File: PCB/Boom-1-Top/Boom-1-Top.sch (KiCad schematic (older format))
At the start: 983 parts, among them J1 DEBUG, J10 PIC_DEBUG, J11 PIC_DEBUG, J12 PIC_DEBUG, J13 PIC_DEBUG, J14 PIC_DEBUG, J15 USB_B_Micro, J16 SD_Card, J17 BT_DEBUG, J18 12V Supply, J19 3V3 Bypass, J2 MIDI IN, J20 5V Bypass, J21 Env +12V Supply, J22 Env -12V Supply, J23 OLEDConn, J3 MIDI OUT, J37 Osc1Conn, J38 Osc2Conn, J39 SubNoiseConn, J4 PIC_DEBUG, J40 FiltConn2, J41 EnvGenConn2, J42 EnvGenConn1, J43 FXConn1, J44 FiltConn1, J45 FXConn2, J46 EnvGenConn3, J5 PIC_DEBUG, J6 PIC_DEBUG, J7 PIC_DEBUG, J8 PIC_DEBUG, J9 PIC_DEBUG, Q1 AO3401A, Q2 AO3401A, SW1 Osc1SawEncoder, SW10 SubToOsc2FiltEncoder, SW11 Osc1ToOsc2FiltEncoder, SW12 Osc1FiltFreqEncoder, SW13 Osc2FiltFreqEncoder, SW14 SubFiltFreqEncoder, SW15 OscFiltEnvAttackEncoder, SW16 SubFiltEnvAttackEncoder, SW17 Osc1FiltResEncoder, SW18 Osc2FiltResEncoder, SW19 SubFiltResEncoder, SW2 Osc1SqrEncoder, SW20 OscFiltEnvDecayEncoder, SW21 SubFiltEnvDecayEncoder, SW22 OscFiltEnvSustainEncoder, SW23 SubFiltEnvSustainEncoder, SW24 Osc1DriveEncoder, SW25 Osc2DistortionEncoder, SW26 OscFiltEnvReleaseEncoder, SW27 SubFiltEnvReleaseEncoder, SW28 FXWetDryEncoder, SW29 SubAmpEnvAttackEncoder, SW3 Rotary_Encoder, SW30 OscAmpEnvAttackEncoder, SW31 FXControl1Encoder, SW32 SubAmpEnvDecayEncoder, SW33 OscAmpEnvDecayEncoder, SW34 FXControl2Encoder, SW35 SubAmpEnvSustainEncoder, SW36 OscAmpEnvSustainEncoder, SW37 FXControl3Encoder, SW38 FXFeedbackEncoder, SW39 SubAmpEnvReleaseEncoder, SW4 Rotary_Encoder_Switch, SW40 OscAmpEnvReleaseEncoder, SW41 Reset, SW42 SW_Push, SW43 Reset, SW44 SW_Push, SW45 SW_Push, SW46 SW_Push, SW47 SW_Push, SW48 SW_Push, SW49 SW_Push, SW5 Rotary_Encoder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

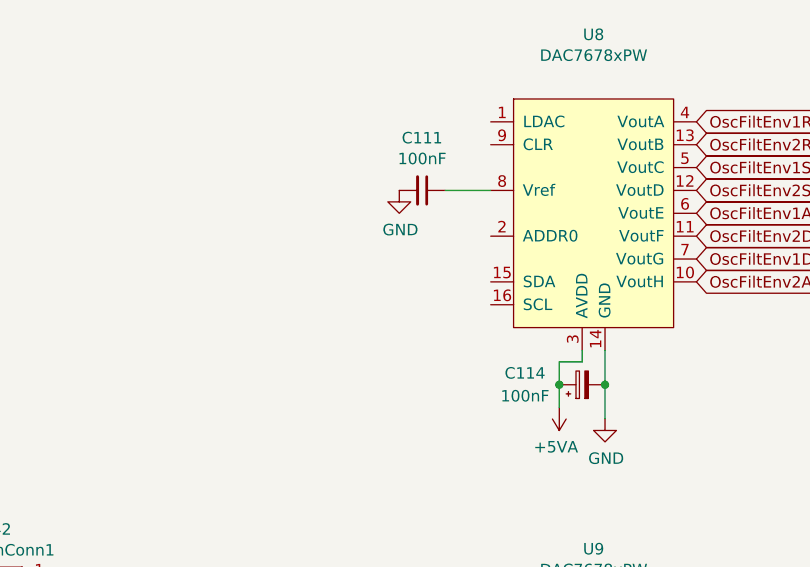
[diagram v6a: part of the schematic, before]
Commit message: U8 DAC i2c
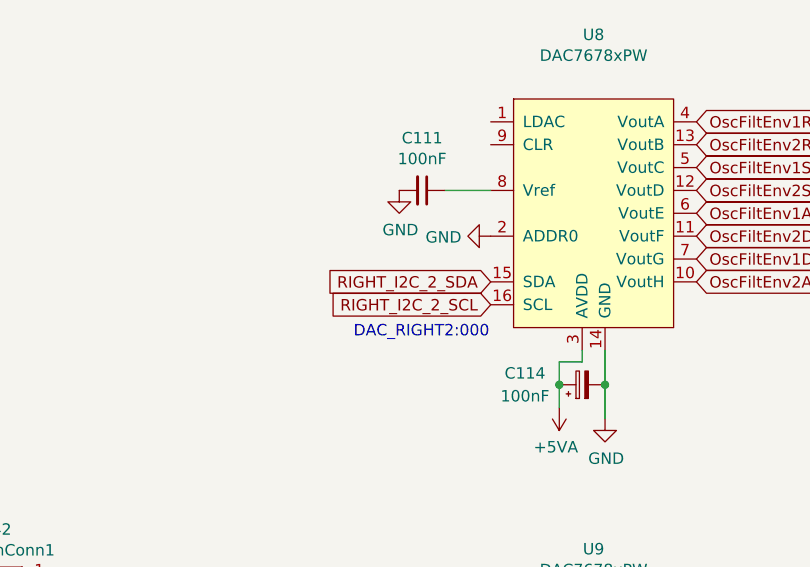
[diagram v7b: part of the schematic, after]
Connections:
- net GND: now also U8.2 (ADDR0)
- net RIGHT_I2C_2_SCL: now also U8.16 (SCL)
- net RIGHT_I2C_2_SDA: now also U8.15 (SDA)
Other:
- note added: "DAC_RIGHT2:000"
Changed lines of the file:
@@
 LEFT_I2C_2_SCL
 $Comp
-L power:GND #PWR?
+L power:GND #PWR0926
 U 1 1 626D0E19
 P 33500 39600
-F 0 "#PWR?" H 33500 39350 50  0001 C CNN
+F 0 "#PWR0926" H 33500 39350 50  0001 C CNN
 F 1 "GND" V 33505 39472 50  0000 R CNN
 F 2 "" H 33500 39600 50  0001 C CNN
@@
 	0    1    1    0
 $EndComp
+Text Notes 39400 37450 0    50   ~ 0
+DAC_RIGHT2:000
+Text GLabel 40000 37200 0    50   Input ~ 0
+RIGHT_I2C_2_SDA
+Text GLabel 40000 37300 0    50   Input ~ 0
+RIGHT_I2C_2_SCL
+$Comp
+L power:GND #PWR?
+U 1 1 62CA8854
+P 40000 37000
+F 0 "#PWR?" H 40000 36750 50  0001 C CNN
+F 1 "GND" V 40005 36872 50  0000 R CNN
+F 2 "" H 40000 37000 50  0001 C CNN
+F 3 "" H 40000 37000 50  0001 C CNN
+	1    40000 37000
+	0    1    1    0
+$EndComp

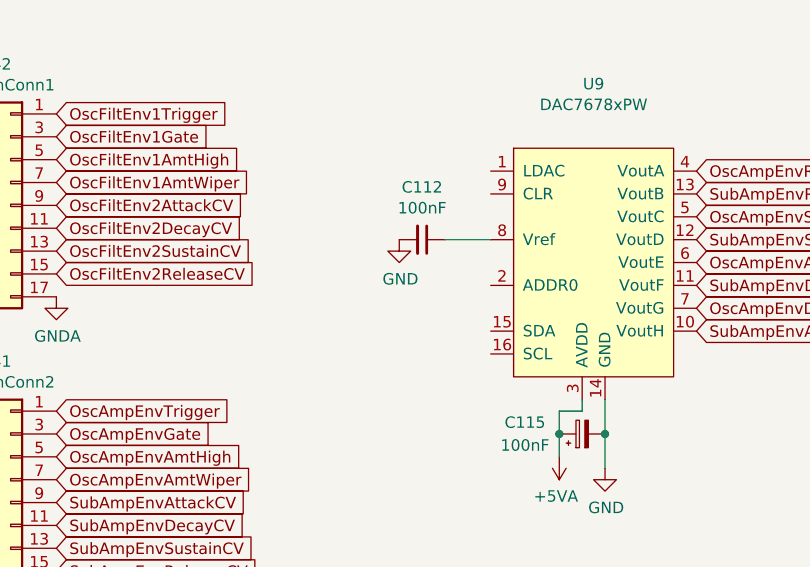
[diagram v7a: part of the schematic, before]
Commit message: U9 DAC i2c
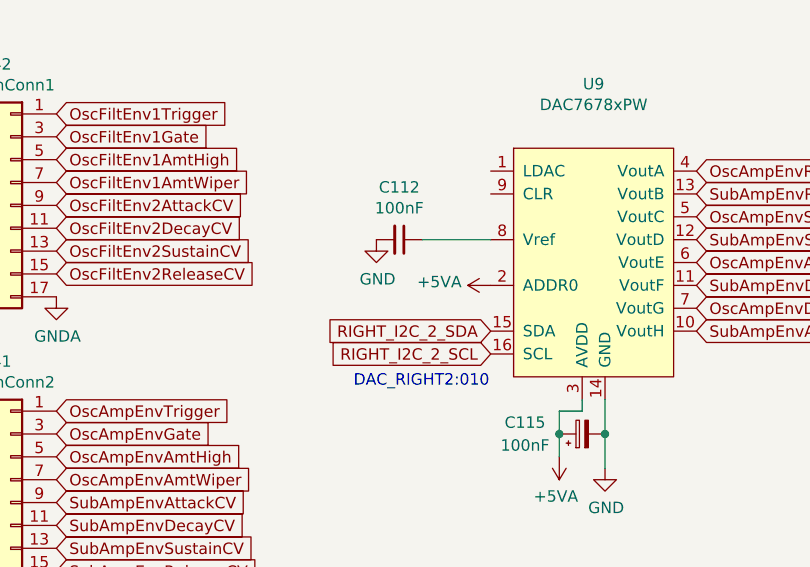
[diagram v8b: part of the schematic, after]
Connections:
- net +5VA: now also U9.2 (ADDR0)
- net RIGHT_I2C_2_SCL: now also U9.16 (SCL)
- net RIGHT_I2C_2_SDA: now also U9.15 (SDA)
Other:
- note added: "DAC_RIGHT2:010"
- moved on the sheet: C112
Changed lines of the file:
@@
 L Device:C_Small C112
 U 1 1 60216401
-P 39700 39050
-F 0 "C112" V 39471 39050 50  0000 C CNN
-F 1 "100nF" V 39562 39050 50  0000 C CNN
-F 2 "Capacitor_SMD:C_0402_1005Metric" H 39700 39050 50  0001 C CNN
-F 3 "~" H 39700 39050 50  0001 C CNN
-	1    39700 39050
+P 39600 39050
+F 0 "C112" V 39371 39050 50  0000 C CNN
+F 1 "100nF" V 39462 39050 50  0000 C CNN
+F 2 "Capacitor_SMD:C_0402_1005Metric" H 39600 39050 50  0001 C CNN
+F 3 "~" H 39600 39050 50  0001 C CNN
+	1    39600 39050
 	0    1    1    0
 $EndComp
@@
 L power:GND #PWR0282
 U 1 1 60216419
-P 39600 39050
-F 0 "#PWR0282" H 39600 38800 50  0001 C CNN
-F 1 "GND" H 39605 38877 50  0000 C CNN
-F 2 "" H 39600 39050 50  0001 C CNN
-F 3 "" H 39600 39050 50  0001 C CNN
-	1    39600 39050
+P 39500 39050
+F 0 "#PWR0282" H 39500 38800 50  0001 C CNN
+F 1 "GND" H 39505 38877 50  0000 C CNN
+F 2 "" H 39500 39050 50  0001 C CNN
+F 3 "" H 39500 39050 50  0001 C CNN
+	1    39500 39050
 	1    0    0    -1
 $EndComp
 Wire Wire Line
-	39800 39050 40000 39050
+	39700 39050 40000 39050
 $Comp
 L Device:C_Small C113
@@
 RIGHT_I2C_2_SCL
 $Comp
-L power:GND #PWR?
+L power:GND #PWR0927
 U 1 1 62CA8854
 P 40000 37000
-F 0 "#PWR?" H 40000 36750 50  0001 C CNN
+F 0 "#PWR0927" H 40000 36750 50  0001 C CNN
 F 1 "GND" V 40005 36872 50  0000 R CNN
 F 2 "" H 40000 37000 50  0001 C CNN
@@
 	0    1    1    0
 $EndComp
+Text Notes 39400 39700 0    50   ~ 0
+DAC_RIGHT2:010
+Text GLabel 40000 39450 0    50   Input ~ 0
+RIGHT_I2C_2_SDA
+Text GLabel 40000 39550 0    50   Input ~ 0
+RIGHT_I2C_2_SCL
+$Comp
+L power:+5VA #PWR?
+U 1 1 63482FFE
+P 40000 39250
+F 0 "#PWR?" H 40000 39100 50  0001 C CNN
+F 1 "+5VA" V 40015 39377 50  0000 L CNN
+F 2 "" H 40000 39250 50  0001 C CNN
+F 3 "" H 40000 39250 50  0001 C CNN
+	1    40000 39250
+	0    -1   -1   0
+$EndComp
 $EndSCHEMATC
